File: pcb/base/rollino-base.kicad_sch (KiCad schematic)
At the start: 7 parts, among them J1 FH12-6S-0.5SH, J2 FH12-6S-0.5SH, U1 XIAO nRF52840

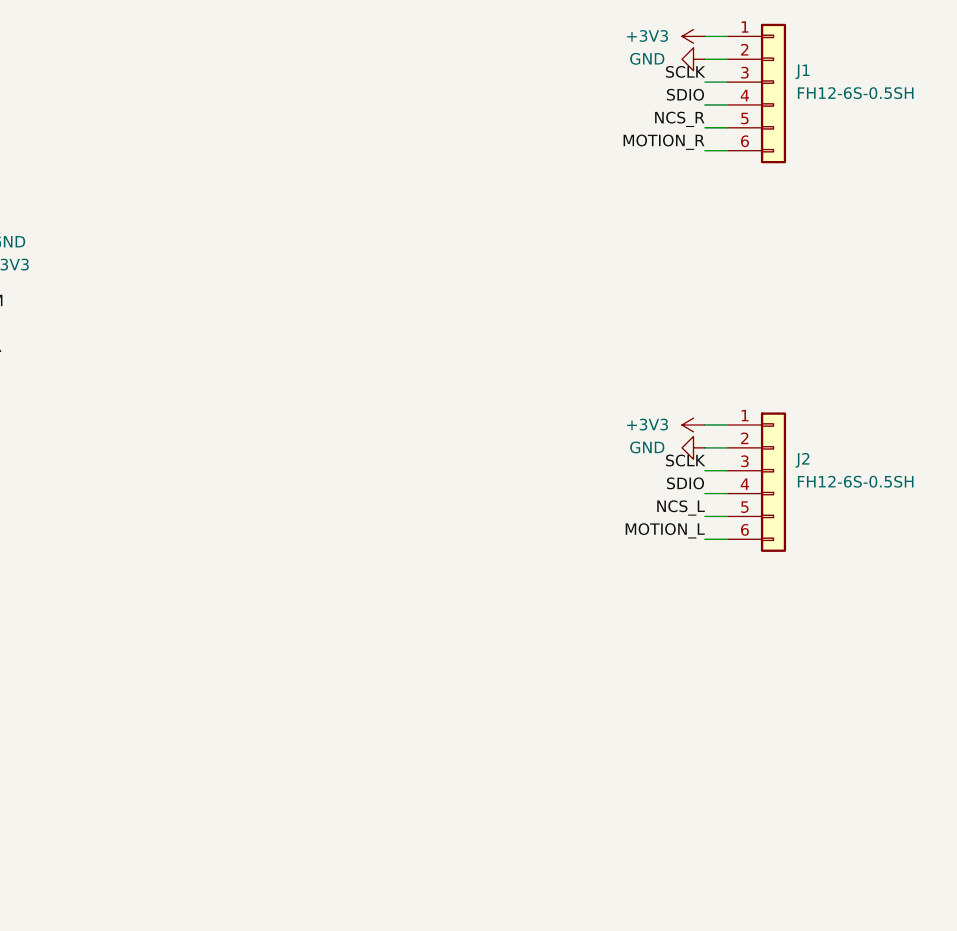
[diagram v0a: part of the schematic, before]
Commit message: Route both PCBs, copper logo, 3D renders of the boards
pcb/gen/route.py has Freerouting route every net (edge and logo keep-outs,
retrying strategies until nothing is left unconnected) and pours GND;
pcb/gen/render_pcbs.sh renders both boards in Blender from KiCad's VRML,
with generated models for the upside-down XIAO and the PMW3610 + lens. The
ROLLINO logo is now bare copper on the back of the band instead of
silkscreen cut by the XIAO's cutout. Connector mounting tabs go to GND;
mounting holes have symbols; the band is 0.5 mm wider for the connectors'
escape routes.

Co-Authored-By: Claude Opus 5.5 <noreply@anthropic.com>
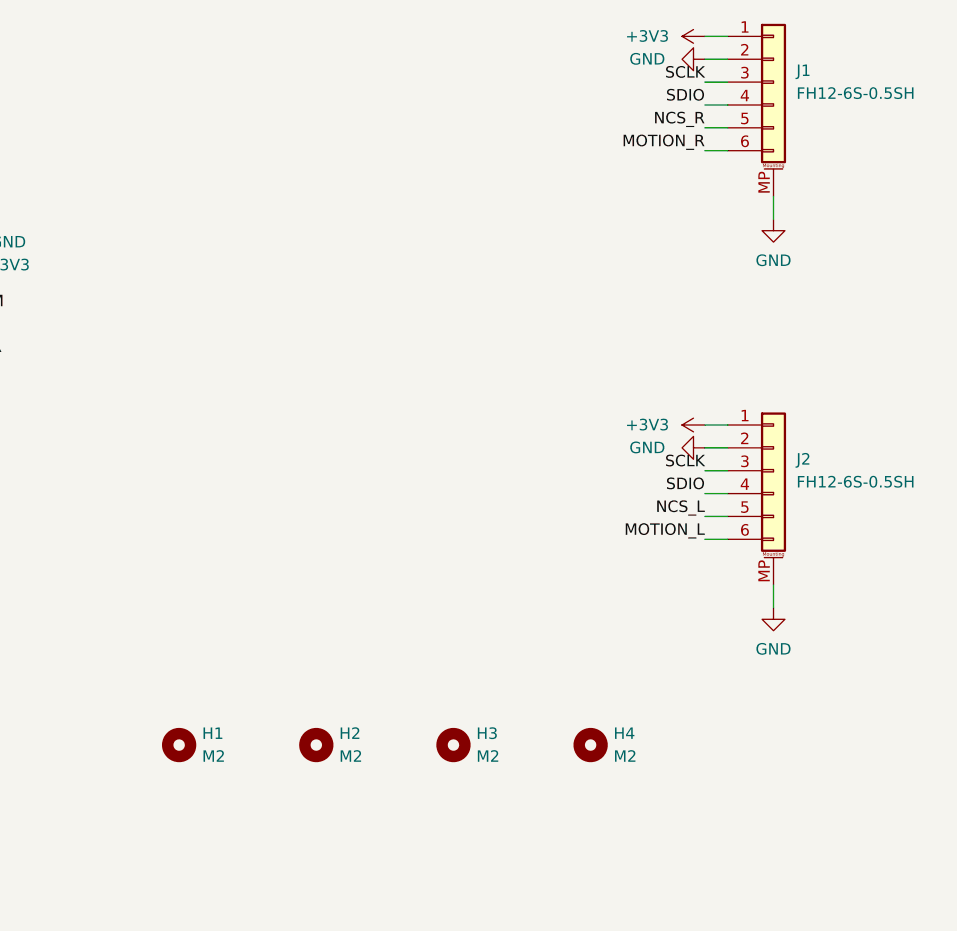
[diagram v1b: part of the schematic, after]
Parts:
- removed J1, J2: FH12-6S-0.5SH, Connector_FFC-FPC:Hirose_FH12-6S-0.5SH_1x06-1MP_P0.50mm_Horizontal, symbol Connector_Generic:Conn_01x06
- added H1, H2, H3, H4: M2, MountingHole:MountingHole_2.2mm_M2, symbol Mechanical:MountingHole
- added J1, J2: FH12-6S-0.5SH, Connector_FFC-FPC:Hirose_FH12-6S-0.5SH_1x06-1MP_P0.50mm_Horizontal, symbol Connector_Generic_MountingPin:Conn_01x06_MountingPin
- TP1, TP2, TP3, TP4: now left out of the parts list
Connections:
- net +3V3: now also J1.1 (Pin_1), J2.1 (Pin_1)
- net GND: now also J1.2 (Pin_2), J1.MP (MountPin), J2.2 (Pin_2), J2.MP (MountPin)
- net MOTION_L: now also J2.6 (Pin_6)
- net MOTION_R: now also J1.6 (Pin_6)
- net NCS_L: now also J2.5 (Pin_5)
- net NCS_R: now also J1.5 (Pin_5)
- net SCLK: now also J1.3 (Pin_3), J2.3 (Pin_3)
- net SDIO: now also J1.4 (Pin_4), J2.4 (Pin_4)

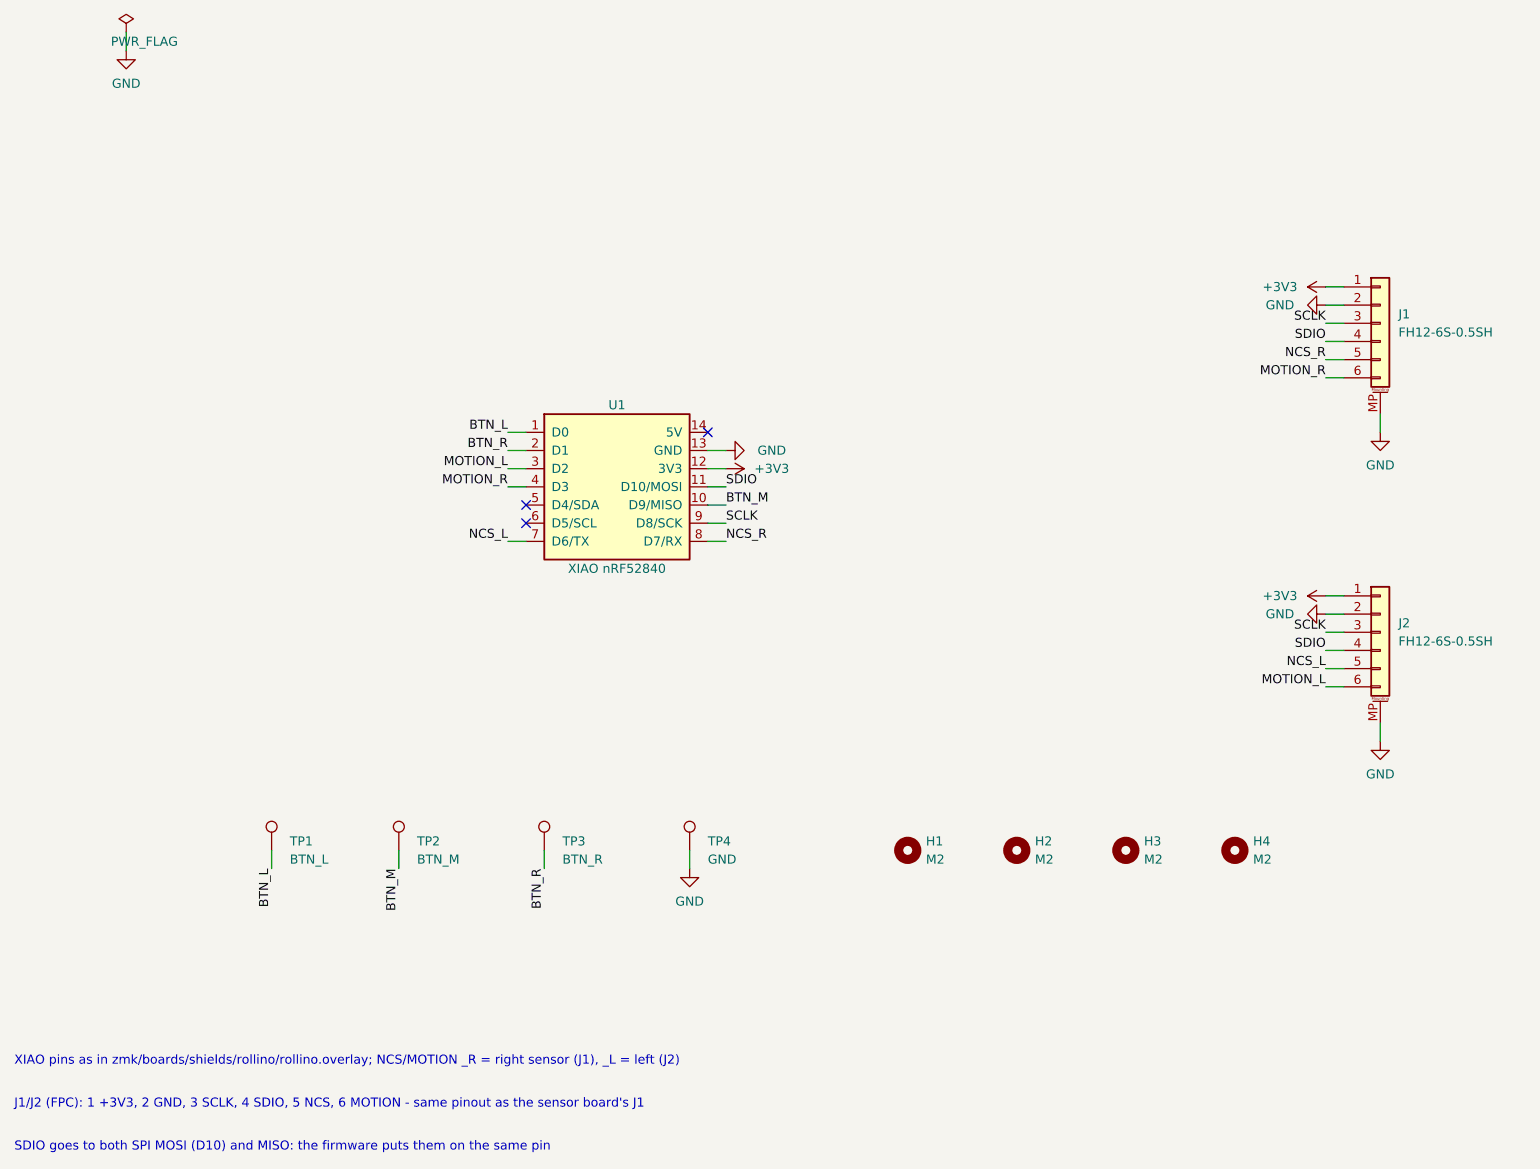
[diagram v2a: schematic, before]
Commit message: Shorter base band for a stock 50 mm FFC, parts list, FPC pin order fix
The base board's band now ends at about 110 degrees, with the FPC
connectors lying along it; each ribbon creases flat under its sensor pod
and runs along a channel in the case's underside, held by the cover.
The model solves the crease position from fpc_len = 50 (type B cable).
Connector pins are numbered from the ribbon's path so each signal meets
itself (the flipped sensor connector had reversed them).
Adds parts.md, the parts to order.

Co-Authored-By: Claude Opus 5.5 <noreply@anthropic.com>
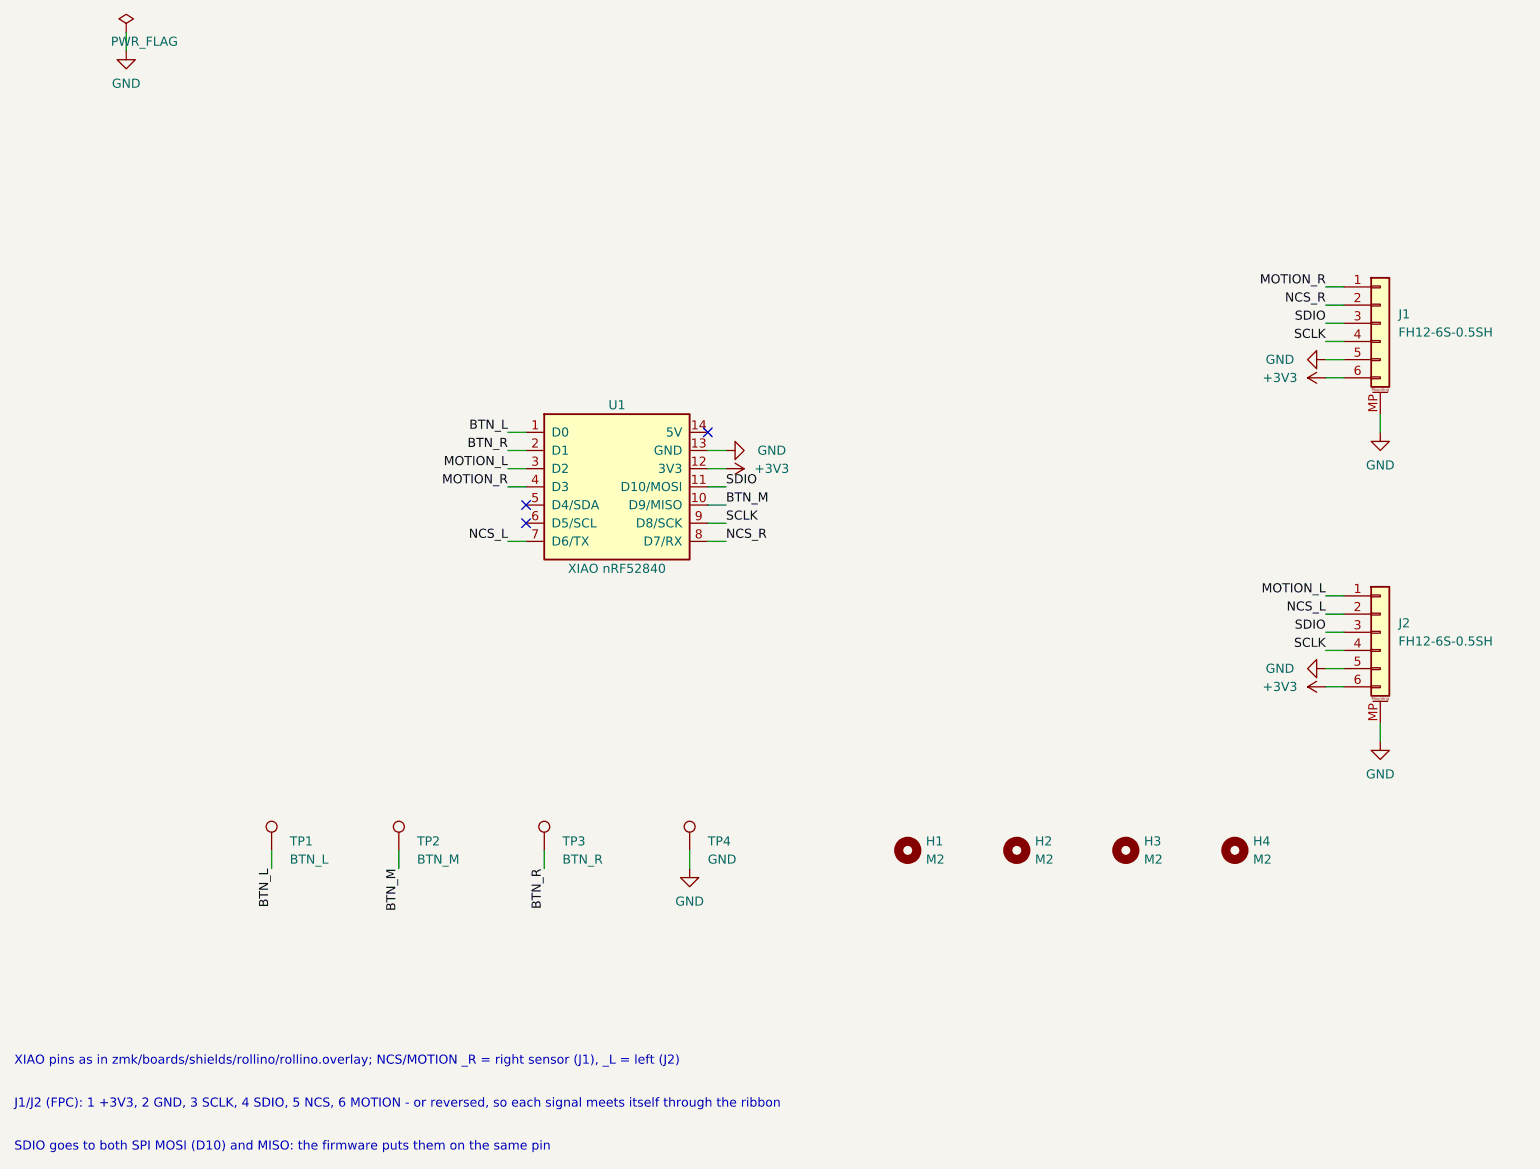
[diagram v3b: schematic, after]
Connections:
- net +3V3: now also J1.6 (Pin_6), J2.6 (Pin_6); no longer J1.1 (Pin_1), J2.1 (Pin_1)
- net GND: now also J1.5 (Pin_5), J2.5 (Pin_5); no longer J1.2 (Pin_2), J2.2 (Pin_2)
- net MOTION_L: now also J2.1 (Pin_1); no longer J2.6 (Pin_6)
- net MOTION_R: now also J1.1 (Pin_1); no longer J1.6 (Pin_6)
- net NCS_L: now also J2.2 (Pin_2); no longer J2.5 (Pin_5)
- net NCS_R: now also J1.2 (Pin_2); no longer J1.5 (Pin_5)
- net SCLK: now also J1.4 (Pin_4), J2.4 (Pin_4); no longer J1.3 (Pin_3), J2.3 (Pin_3)
- net SDIO: now also J1.3 (Pin_3), J2.3 (Pin_3); no longer J1.4 (Pin_4), J2.4 (Pin_4)
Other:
- note added: "J1/J2 (FPC): 1 +3V3, 2 GND, 3 SCLK, 4 SDIO, 5 NCS, 6 MOTION - or reversed, so each signal meets itself through the ribbon"
- note removed: "J1/J2 (FPC): 1 +3V3, 2 GND, 3 SCLK, 4 SDIO, 5 NCS, 6 MOTION - same pinout as the sensor board's J1"

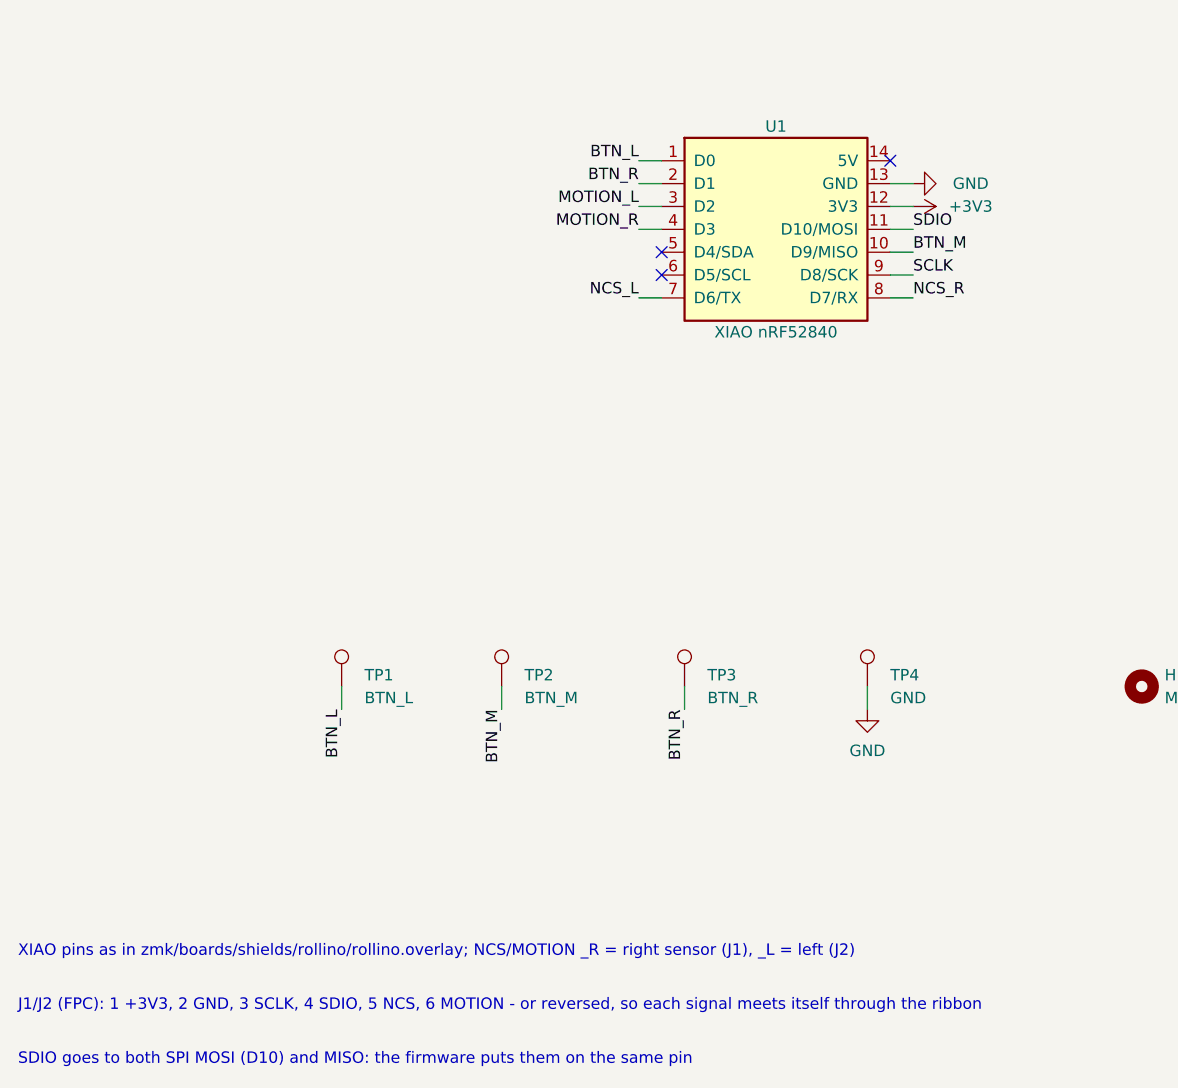
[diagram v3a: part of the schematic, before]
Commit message: Route the base board again, clear the antenna, sensor decoupling by the pins
The base board had come out with nothing routed to its FPC connectors:
Freerouting can't start a track from their pads at this angle. generate.py
now lays a stub out of each pad and route.py has Freerouting join those;
route.py only saves a board that is whole and that KiCad's DRC has nothing
to report on, trying its other strategies otherwise.

Base board: no pour by the XIAO's antenna (the strip between the notch and
the ball's hole), the supply laid across that strip on the back, each
connector's grounds with their own vias to the pours, the pours stitched
together. The bus moves to D4/D5 (the XIAO's only pins that aren't kept
for low frequencies), the right sensor's MOTION to D8, and the buttons are
left, middle, right on D0, D1, D9, so each side's lines stay on its side.

Sensor board: each capacitor by the pin it serves on a short wide track
(PixArt's rule for CP, CN and VCP), the regulator's output capacitor
against it, a ground rail with vias from pin 11, 1.8 V round the lens
cutout on the back, test pads for 1.8 V and GND. Same parts.

Firmware: the new pins, the sensors' angles as the case model has them
now (elevation -22), full transmit power. Case: a hole in the cover under
the XIAO's reset button. The XIAO's 3D model on the base board was a
mirror image.

Co-Authored-By: Claude Opus 5.5 <noreply@anthropic.com>
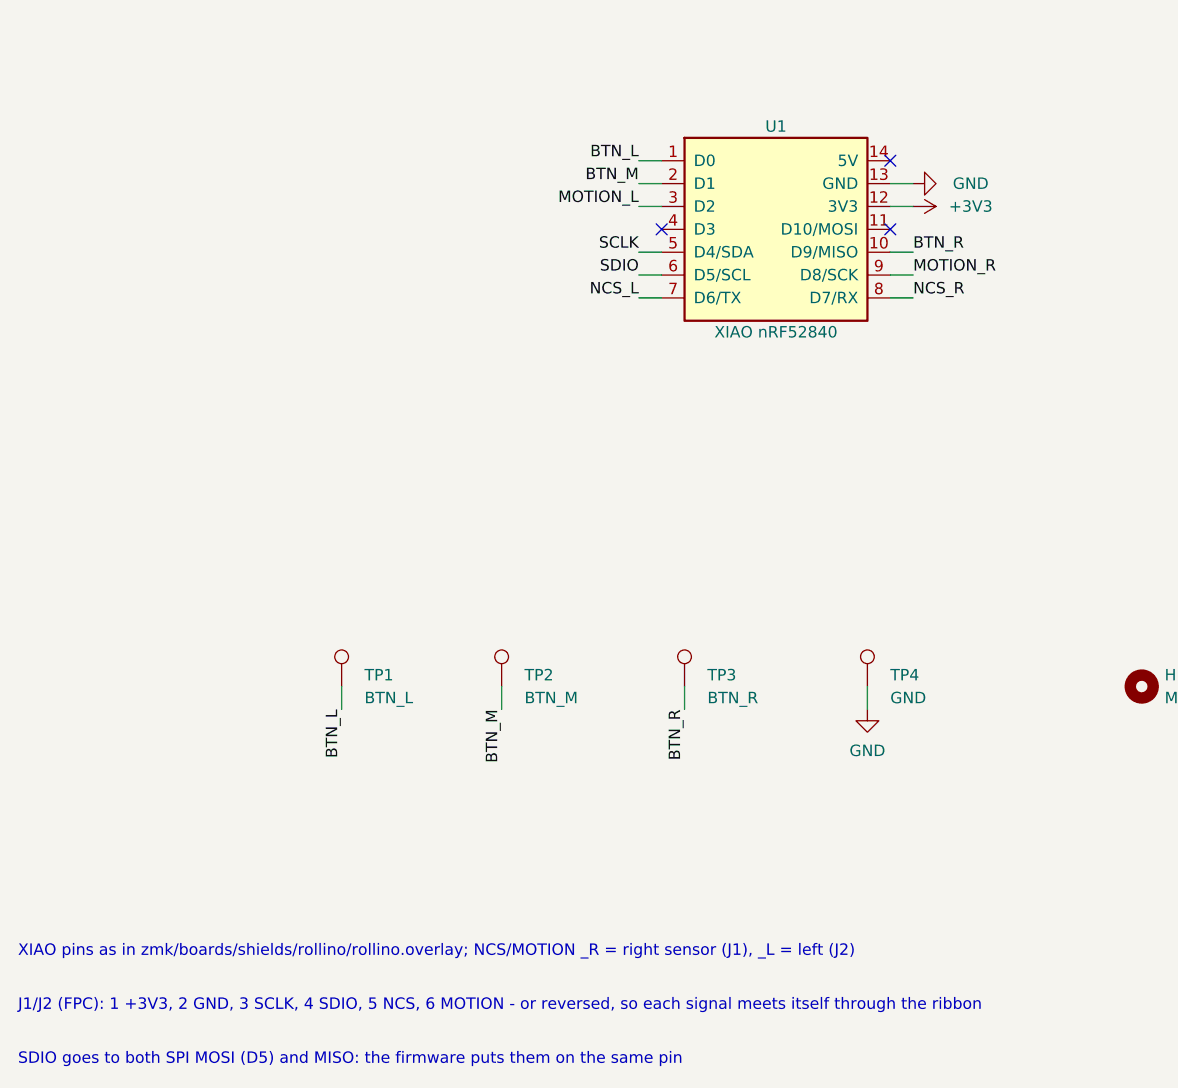
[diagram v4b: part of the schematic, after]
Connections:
- net BTN_M: now also U1.2 (D1); no longer U1.10 (D9/MISO)
- net BTN_R: now also U1.10 (D9/MISO); no longer U1.2 (D1)
- net MOTION_R: now also U1.9 (D8/SCK); no longer U1.4 (D3)
- net SCLK: now also U1.5 (D4/SDA); no longer U1.9 (D8/SCK)
- net SDIO: now also U1.6 (D5/SCL); no longer U1.11 (D10/MOSI)
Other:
- note added: "SDIO goes to both SPI MOSI (D5) and MISO: the firmware puts them on the same pin"
- note removed: "SDIO goes to both SPI MOSI (D10) and MISO: the firmware puts them on the same pin"
